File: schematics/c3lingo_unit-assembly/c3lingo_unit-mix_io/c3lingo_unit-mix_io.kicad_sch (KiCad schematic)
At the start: 45 parts, among them J201 Stage Line-In, J202 Mix Line-Out, J203 PowerSupply, J204 Ch1, J205 Ch2, J206 Ch3, SW201 GND Lift, U201 LM833-N, U202 DRV135UA, U203 LM833-N

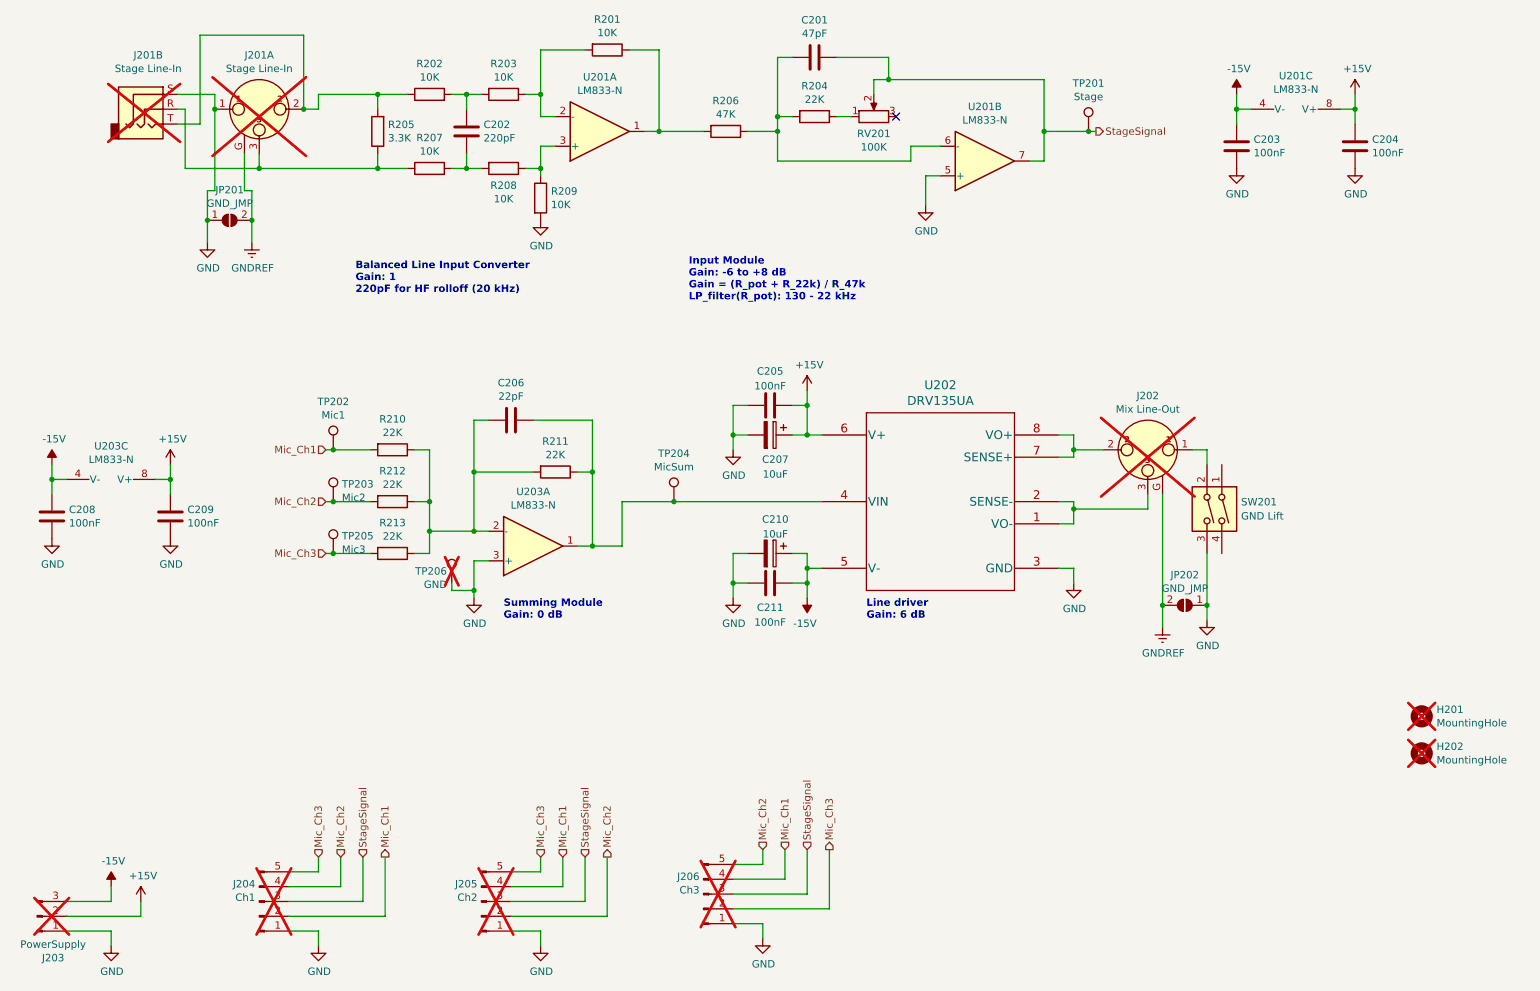
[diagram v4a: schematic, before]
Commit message: Tidy: Rename hierarchical labels
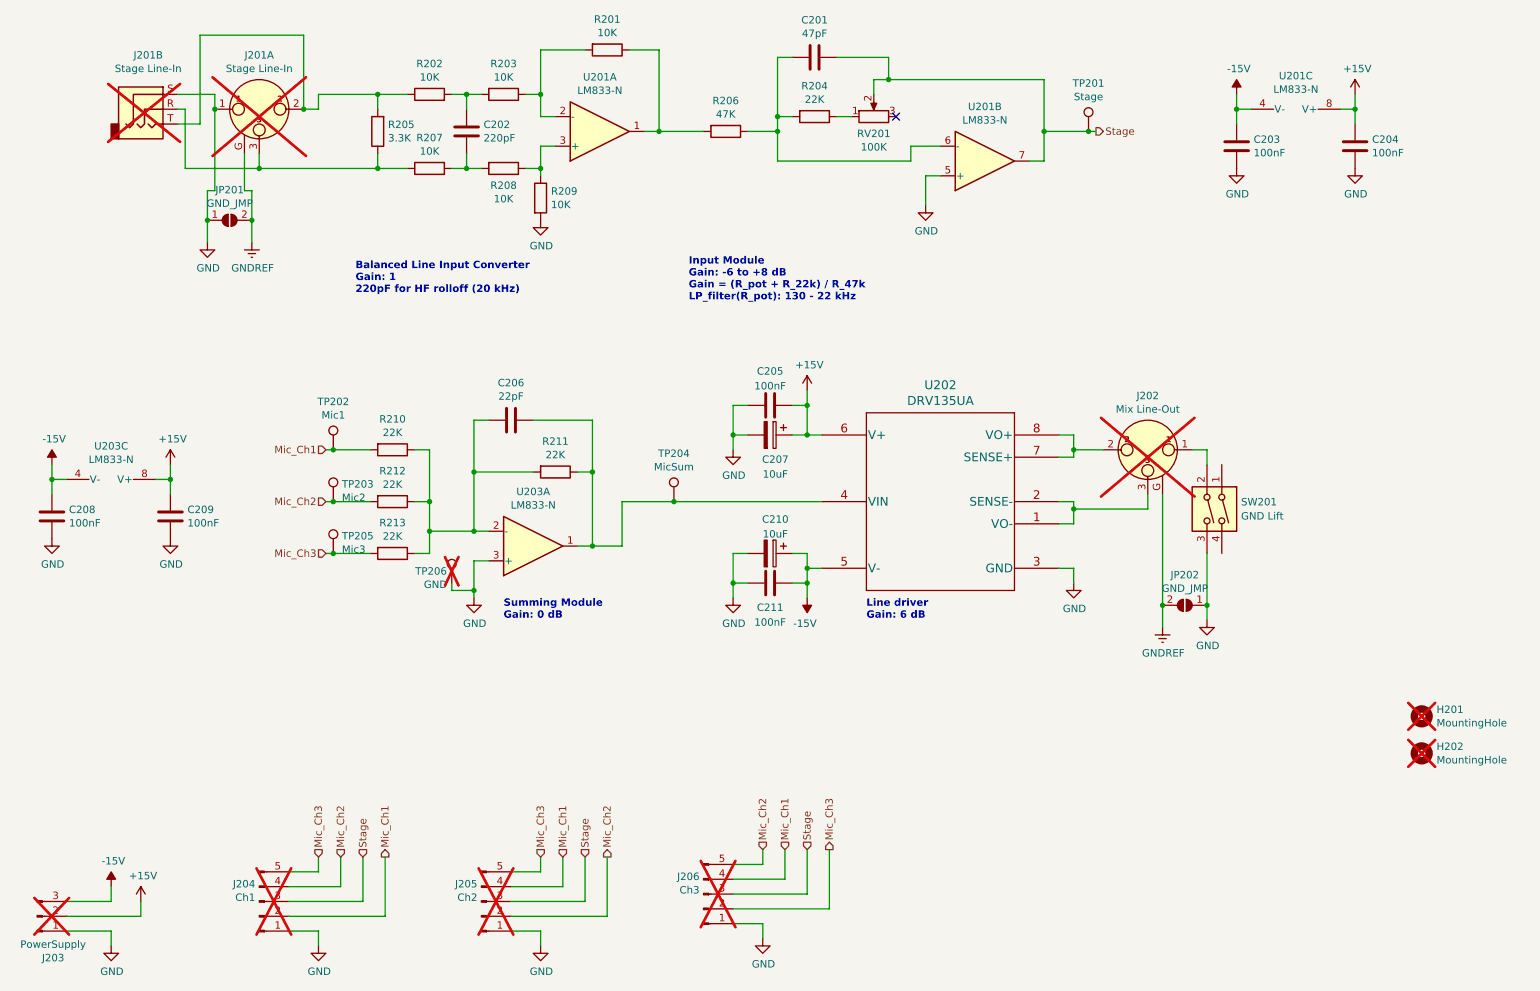
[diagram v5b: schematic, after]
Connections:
- net StageSignal renamed Stage
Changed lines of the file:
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@@
 		)
 	)
-	(hierarchical_label "StageSignal"
+	(hierarchical_label "Stage"
 		(shape input)
 		(at 157.48 173.99 90)
@@
 		)
 	)
-	(hierarchical_label "StageSignal"
+	(hierarchical_label "Stage"
 		(shape input)
 		(at 119.38 175.26 90)
@@
 		)
 	)
-	(hierarchical_label "StageSignal"
+	(hierarchical_label "Stage"
 		(shape input)
 		(at 81.28 175.26 90)
@@
 		)
 	)
-	(hierarchical_label "StageSignal"
+	(hierarchical_label "Stage"
 		(shape output)
 		(at 207.01 50.8 0)

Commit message: Channel Mixer: Rework muting mechanism
Note: Schematic PDF not updated yet
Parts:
- C207, C210: footprint Capacitor_SMD:C_Elec_4x5.4 -> Capacitor_SMD:CP_Elec_4x5.4
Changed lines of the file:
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@@
 	(title_block
 		(title "c3lingo interpeter unit -- mix and line I/O")
-		(date "2024-07-08")
+		(date "2024-08-30")
 		(rev "v0.3.1")
 		(company "Jannik Beyerstedt (jtbx)")
@@
 			)
 		)
-		(property "Footprint" "Capacitor_SMD:C_Elec_4x5.4"
+		(property "Footprint" "Capacitor_SMD:CP_Elec_4x5.4"
 			(at 147.32 124.1552 0)
 			(effects
@@
 			)
 		)
-		(property "Footprint" "Capacitor_SMD:C_Elec_4x5.4"
+		(property "Footprint" "Capacitor_SMD:CP_Elec_4x5.4"
 			(at 147.32 103.8352 0)
 			(effects

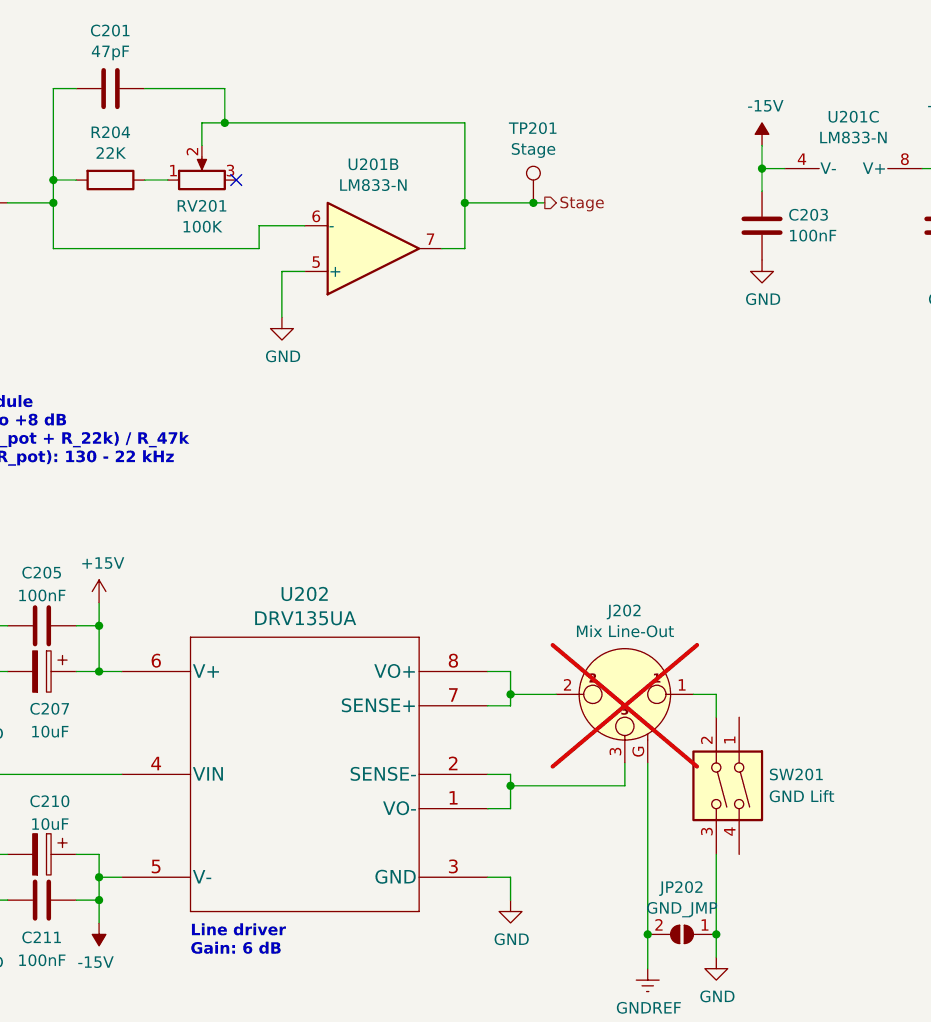
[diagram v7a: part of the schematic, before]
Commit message: Move potentiometers down, fix JLC PCB components
- Fix JLC PCB component orientation
- Add do-not-populate to all THD components
- Fix JLC part selection, tweak values to be standard components
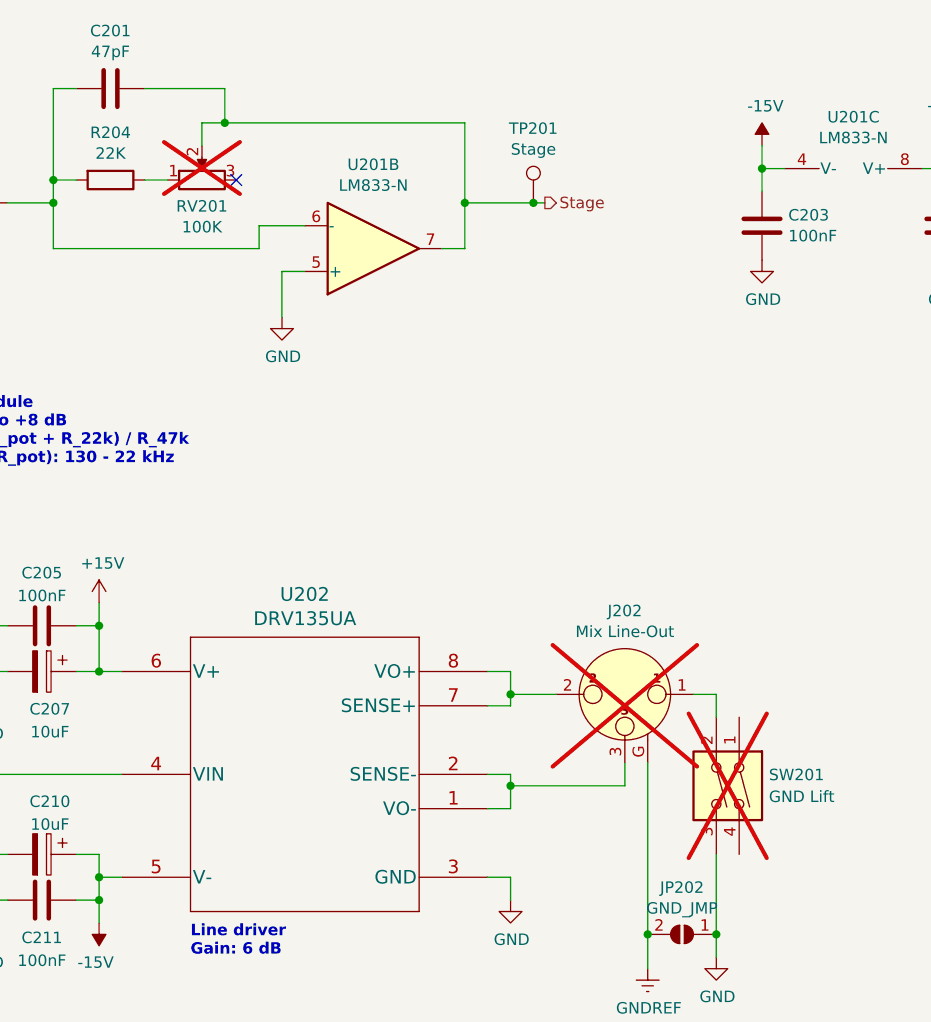
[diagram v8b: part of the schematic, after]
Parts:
- C207, C210: JLCPCB Rotation Offset (none) -> 180; LCSC Part # C3001226 -> C3343
- RV201, SW201: now not fitted
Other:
- title: c3lingo interpeter unit -- mix and line I/O -> c3lingo interpeter unit -- main I/O
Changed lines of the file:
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@@
 	(paper "A4")
 	(title_block
-		(title "c3lingo interpeter unit -- mix and line I/O")
-		(date "2024-09-06")
-		(rev "v0.3.2")
+		(title "c3lingo interpeter unit -- main I/O")
+		(date "2024-09-08")
+		(rev "v0.3.3")
 		(company "Jannik Beyerstedt (jtbx)")
 		(comment 1 "Prototype 2")
@@
 		(in_bom yes)
 		(on_board yes)
-		(dnp no)
+		(dnp yes)
 		(property "Reference" "RV201"
 			(at 168.91 51.181 90)
@@
 			)
 		)
-		(property "LCSC Part #" "C3001226"
+		(property "LCSC Part #" "C3343"
 			(at 151.13 123.19 0)
 			(effects
@@
 			)
 		)
+		(property "JLCPCB Rotation Offset" "180"
+			(at 151.13 123.19 90)
+			(effects
+				(font
+					(size 1.27 1.27)
+				)
+				(hide yes)
+			)
+		)
 		(pin "1"
 		)
@@
 		(in_bom yes)
 		(on_board yes)
-		(dnp no)
+		(dnp yes)
 		(fields_autoplaced yes)
 		(property "Reference" "SW201"
@@
 			)
 		)
-		(property "LCSC Part #" "C3001226"
+		(property "LCSC Part #" "C3343"
+			(at 151.13 102.87 0)
+			(effects
+				(font
+					(size 1.27 1.27)
+				)
+				(hide yes)
+			)
+		)
+		(property "JLCPCB Rotation Offset" "180"
 			(at 151.13 102.87 0)
 			(effects
